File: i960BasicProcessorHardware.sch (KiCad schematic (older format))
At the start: 66 parts, among them J1 Conn_01x08, J10 Conn_01x03, J2 Conn_02x39_Odd_Even, J3 Conn_01x03, J4 Conn_02x05_Odd_Even, J5 Conn_02x05_Odd_Even, J6 Conn_02x05_Odd_Even, J7 Conn_01x06, J8 Conn_01x06, J9 Conn_01x12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

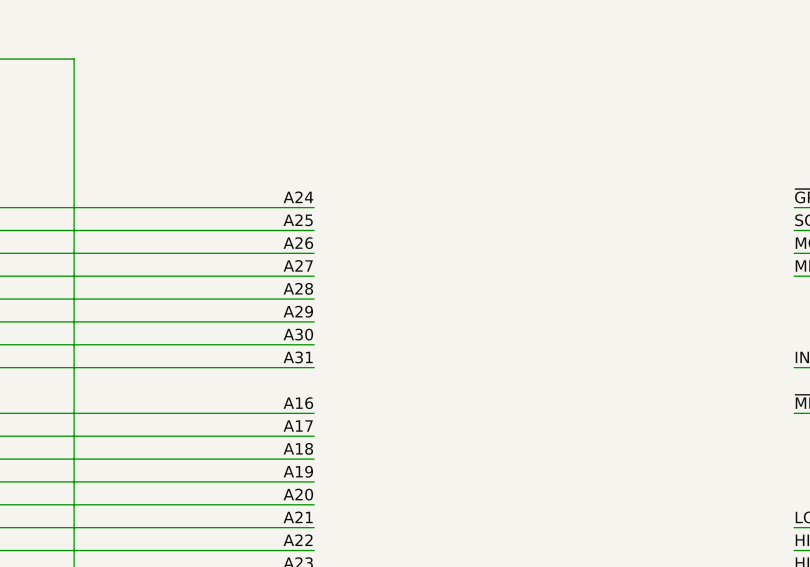
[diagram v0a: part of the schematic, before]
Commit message: Decided to break the highest 8 bits of the address out to a separate header.
I've done it before when I made the processor card interface. I can
position it fairly close without fear of signal degredation
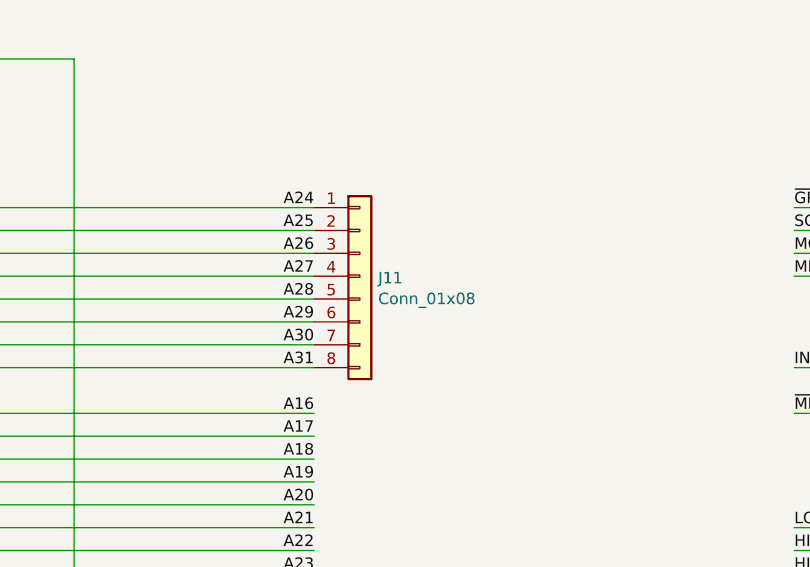
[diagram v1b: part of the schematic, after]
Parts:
- added J11: Conn_01x08, Connector_PinHeader_2.54mm:PinHeader_1x08_P2.54mm_Vertical, symbol Connector_Generic:Conn_01x08
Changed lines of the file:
@@
 NoConn ~ 14900 16000
 NoConn ~ 14900 16100
+$Comp
+L Connector_Generic:Conn_01x08 J11
+U 1 1 782AFBD5
+P 9000 16000
+F 0 "J11" H 9080 15992 50  0000 L CNN
+F 1 "Conn_01x08" H 9080 15901 50  0000 L CNN
+F 2 "Connector_PinHeader_2.54mm:PinHeader_1x08_P2.54mm_Vertical" H 9000 16000 50  0001 C CNN
+F 3 "~" H 9000 16000 50  0001 C CNN
+	1    9000 16000
+	1    0    0    -1
+$EndComp
 $EndSCHEMATC

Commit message: Rearrange some of the board and move the interrupt pull ups to individual resistors
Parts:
- added R3, R5: 10k, Resistor_SMD:R_0805_2012Metric_Pad1.20x1.40mm_HandSolder, symbol Device:R
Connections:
- wire segments 726 -> 730
- no-connect marks 89 -> 91
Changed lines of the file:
@@
 ALE
-Wire Wire Line
-	19200 17700 18200 17700
-Wire Wire Line
-	19200 17600 18200 17600
-Wire Wire Line
-	19200 17500 18200 17500
-Text Label 18200 17700 0    50   ~ 0
-BA1
-Text Label 18200 17600 0    50   ~ 0
-BA2
-Text Label 18200 17500 0    50   ~ 0
-BA3
 Wire Wire Line
 	13450 15800 14900 15800
@@
 Text Label 28000 21350 1    50   ~ 0
 ~RESET960
-Wire Wire Line
-	27600 20400 27600 21350
-Wire Wire Line
-	27500 20400 27500 21350
-Text Label 27500 21350 1    50   ~ 0
-~INT3
-Text Label 27600 21350 1    50   ~ 0
-~INT0
 Text Label 16050 15800 0    50   ~ 0
 GPA0
@@
 $EndComp
 Wire Wire Line
-	19200 17800 18200 17800
-Wire Wire Line
-	19200 17900 18200 17900
-Wire Wire Line
 	19200 17200 18200 17200
-Wire Wire Line
-	19200 18000 18200 18000
-Wire Wire Line
-	19200 18100 18200 18100
-Text Label 18200 17800 0    50   ~ 0
-HOLD_BREAKOUT
-Text Label 18200 17900 0    50   ~ 0
-HLDA
-Text Label 18200 18100 0    50   ~ 0
-~INT3
 NoConn ~ 14900 15800
 NoConn ~ 14900 15900
@@
 Text Label 15950 19000 0    50   ~ 0
 INT2_BREAKOUT
-Text Label 18200 18000 0    50   ~ 0
-INT2_BREAKOUT
 NoConn ~ 14900 16000
 NoConn ~ 14900 16100
@@
 	1    0    0    -1
 $EndComp
+Wire Wire Line
+	19200 17800 18200 17800
+Wire Wire Line
+	19200 17900 18200 17900
+Wire Wire Line
+	19200 18100 18200 18100
+Wire Wire Line
+	19200 18000 18200 18000
+Text Label 18200 17800 0    50   ~ 0
+HOLD_BREAKOUT
+Text Label 18200 17900 0    50   ~ 0
+HLDA
+Text Label 18200 18000 0    50   ~ 0
+~INT3
+Text Label 18200 18100 0    50   ~ 0
+INT2_BREAKOUT
+Text Label 18200 17500 0    50   ~ 0
+BA3
+Text Label 18200 17600 0    50   ~ 0
+BA2
+Text Label 18200 17700 0    50   ~ 0
+BA1
+Wire Wire Line
+	19200 17500 18200 17500
+Wire Wire Line
+	19200 17600 18200 17600
+Wire Wire Line
+	19200 17700 18200 17700
+$Comp
+L Device:R R?
+U 1 1 78683F66
+P 20800 12800
+AR Path="/629FB5E8/78683F66" Ref="R?"  Part="1"
+AR Path="/78683F66" Ref="R3"  Part="1"
+F 0 "R3" H 20870 12846 50  0000 L CNN
+F 1 "10k" H 20870 12755 50  0000 L CNN
+F 2 "Resistor_SMD:R_0805_2012Metric_Pad1.20x1.40mm_HandSolder" V 20730 12800 50  0001 C CNN
+F 3 "~" H 20800 12800 50  0001 C CNN
+	1    20800 12800
+	-1   0    0    1
+$EndComp
+Wire Wire Line
+	20800 12950 20800 13750
+$Comp
+L power:+5V #PWR?
+U 1 1 7873D22E
+P 20800 12450
+AR Path="/629FB5E8/7873D22E" Ref="#PWR?"  Part="1"
+AR Path="/7873D22E" Ref="#PWR052"  Part="1"
+F 0 "#PWR052" H 20800 12300 50  0001 C CNN
+F 1 "+5V" H 20815 12623 50  0000 C CNN
+F 2 "" H 20800 12450 50  0001 C CNN
+F 3 "" H 20800 12450 50  0001 C CNN
+	1    20800 12450
+	1    0    0    -1
+$EndComp
+Wire Wire Line
+	20800 12650 20800 12450
+Text Label 20800 13750 1    50   ~ 0
+~INT3
+Wire Wire Line
+	27500 20400 27500 21350
+Wire Wire Line
+	27600 20400 27600 21350
+NoConn ~ 27500 21350
+NoConn ~ 27600 21350
+$Comp
+L Device:R R?
+U 1 1 78AD08ED
+P 21150 12800
+AR Path="/629FB5E8/78AD08ED" Ref="R?"  Part="1"
+AR Path="/78AD08ED" Ref="R5"  Part="1"
+F 0 "R5" H 21220 12846 50  0000 L CNN
+F 1 "10k" H 21220 12755 50  0000 L CNN
+F 2 "Resistor_SMD:R_0805_2012Metric_Pad1.20x1.40mm_HandSolder" V 21080 12800 50  0001 C CNN
+F 3 "~" H 21150 12800 50  0001 C CNN
+	1    21150 12800
+	-1   0    0    1
+$EndComp
+Wire Wire Line
+	21150 12950 21150 13750
+$Comp
+L power:+5V #PWR?
+U 1 1 78AD08F4
+P 21150 12450
+AR Path="/629FB5E8/78AD08F4" Ref="#PWR?"  Part="1"
+AR Path="/78AD08F4" Ref="#PWR060"  Part="1"
+F 0 "#PWR060" H 21150 12300 50  0001 C CNN
+F 1 "+5V" H 21165 12623 50  0000 C CNN
+F 2 "" H 21150 12450 50  0001 C CNN
+F 3 "" H 21150 12450 50  0001 C CNN
+	1    21150 12450
+	1    0    0    -1
+$EndComp
+Wire Wire Line
+	21150 12650 21150 12450
+Text Label 21150 13750 1    50   ~ 0
+~INT0
 $EndSCHEMATC

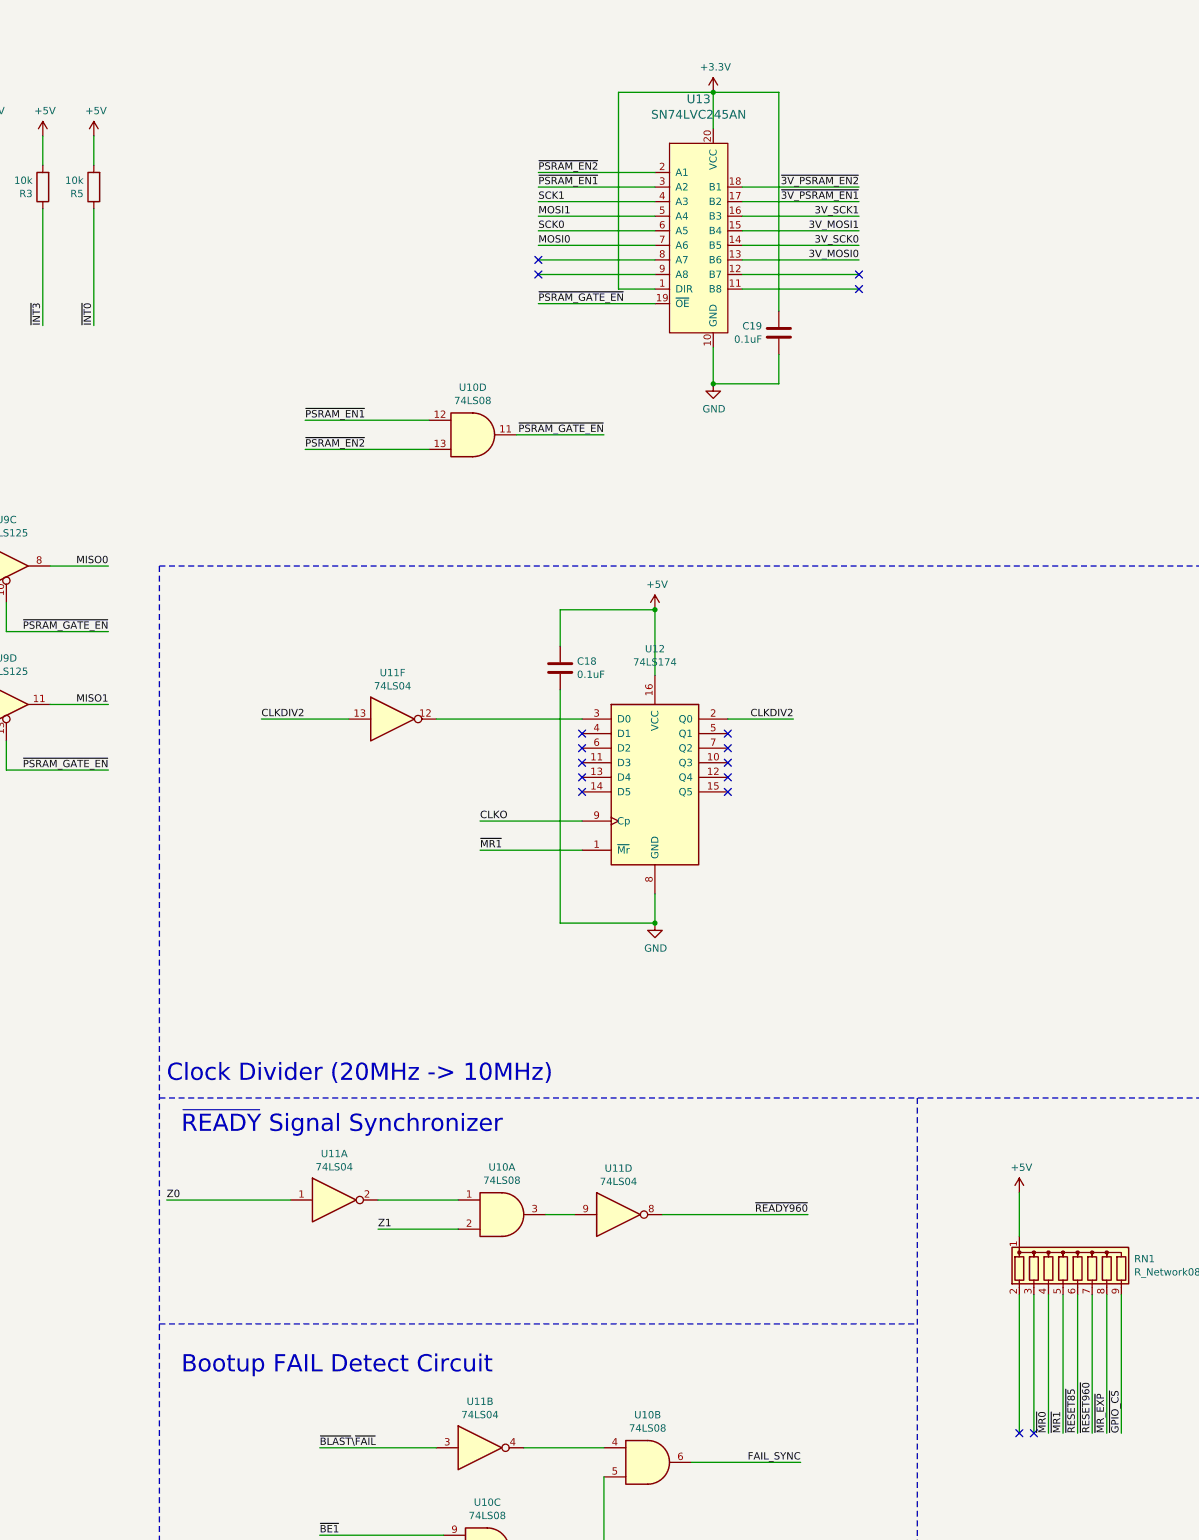
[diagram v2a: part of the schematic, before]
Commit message: Separate ~RESET960's pullup to a separate resistor
I have plenty of space underneath the plcc socket for resistors
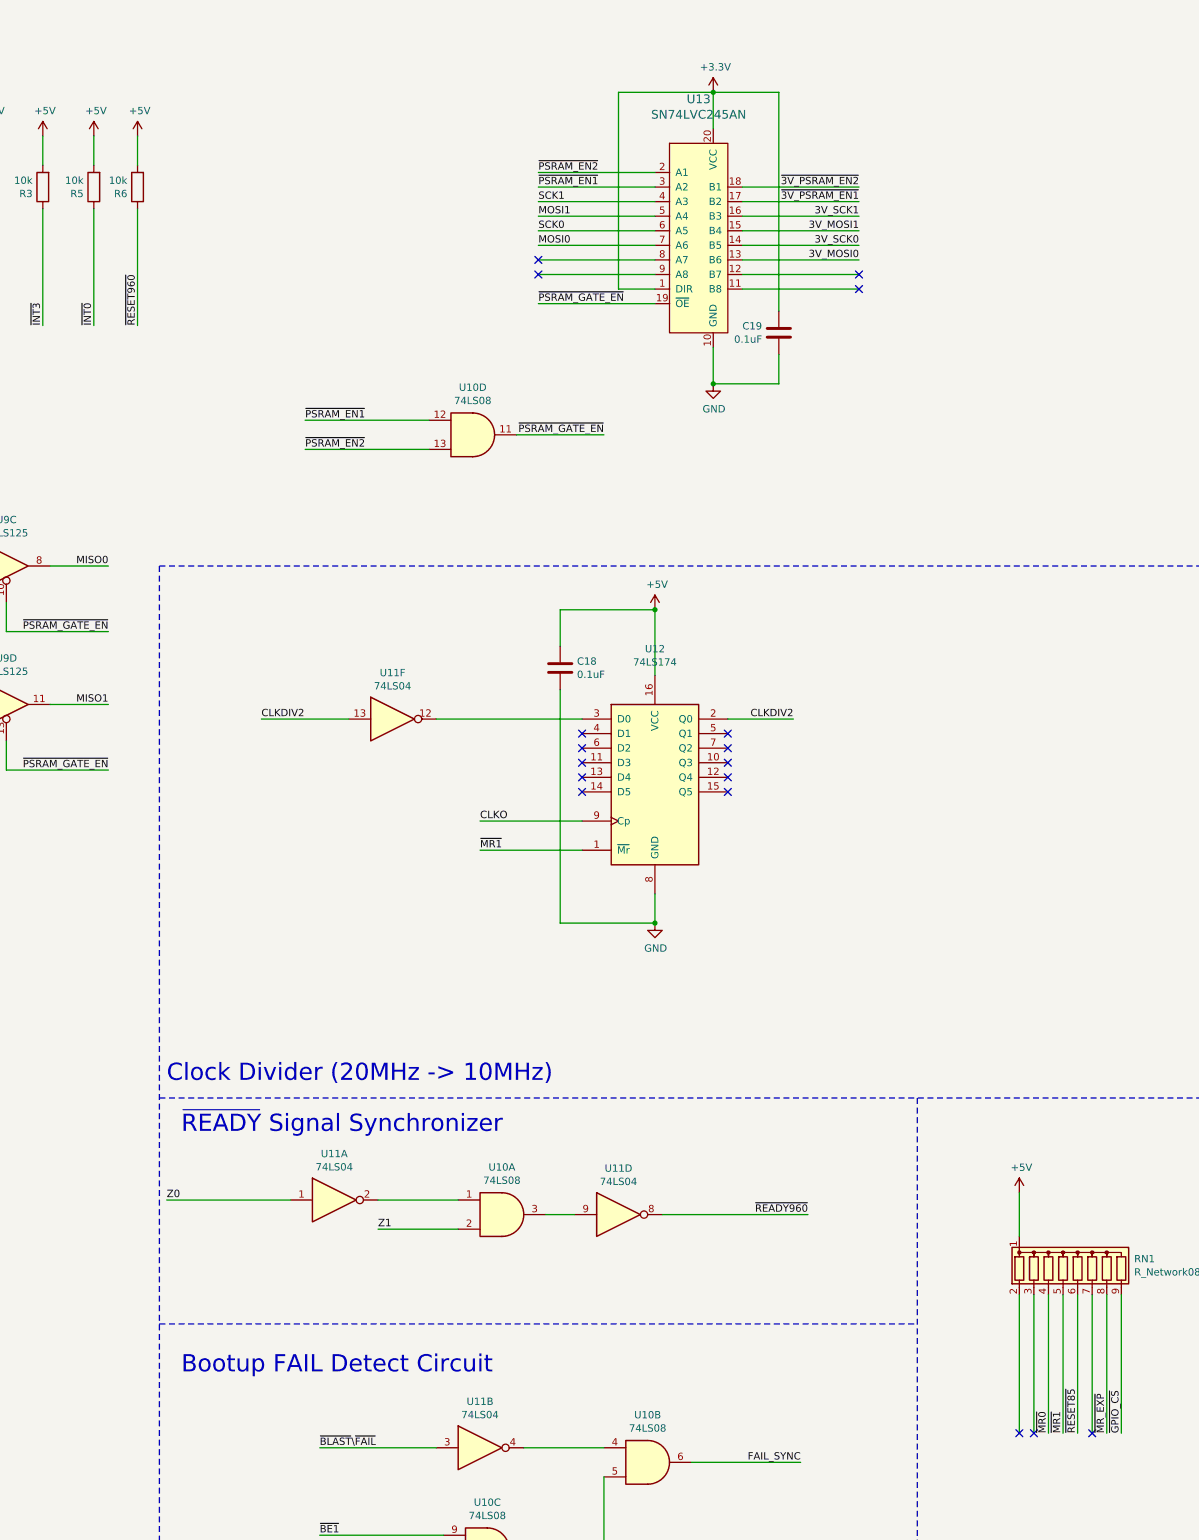
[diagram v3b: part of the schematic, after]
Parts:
- added R6: 10k, Resistor_SMD:R_0805_2012Metric_Pad1.20x1.40mm_HandSolder, symbol Device:R
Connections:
- wire segments 730 -> 732
- no-connect marks 91 -> 92
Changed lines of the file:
@@
 Text Label 28850 3450 0    50   ~ 0
 PA3
-Text Label 28000 21350 1    50   ~ 0
+Text Label 21450 13750 1    50   ~ 0
 ~RESET960
 Text Label 16050 15800 0    50   ~ 0
@@
 Text Label 21150 13750 1    50   ~ 0
 ~INT0
+$Comp
+L Device:R R?
+U 1 1 78BA1B0B
+P 21450 12800
+AR Path="/629FB5E8/78BA1B0B" Ref="R?"  Part="1"
+AR Path="/78BA1B0B" Ref="R6"  Part="1"
+F 0 "R6" H 21520 12846 50  0000 L CNN
+F 1 "10k" H 21520 12755 50  0000 L CNN
+F 2 "Resistor_SMD:R_0805_2012Metric_Pad1.20x1.40mm_HandSolder" V 21380 12800 50  0001 C CNN
+F 3 "~" H 21450 12800 50  0001 C CNN
+	1    21450 12800
+	-1   0    0    1
+$EndComp
+Wire Wire Line
+	21450 12950 21450 13750
+$Comp
+L power:+5V #PWR?
+U 1 1 78BA1B12
+P 21450 12450
+AR Path="/629FB5E8/78BA1B12" Ref="#PWR?"  Part="1"
+AR Path="/78BA1B12" Ref="#PWR061"  Part="1"
+F 0 "#PWR061" H 21450 12300 50  0001 C CNN
+F 1 "+5V" H 21465 12623 50  0000 C CNN
+F 2 "" H 21450 12450 50  0001 C CNN
+F 3 "" H 21450 12450 50  0001 C CNN
+	1    21450 12450
+	1    0    0    -1
+$EndComp
+Wire Wire Line
+	21450 12650 21450 12450
+NoConn ~ 28000 21350
 $EndSCHEMATC

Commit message: move ~RESET960 back to the primary chipset
also move ~INT3 to it as well. I want two different interrupt pins
accessible to the primary chipset. I have made the fourth ioexpander
completely exposed to the i960.
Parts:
- removed J1: Conn_01x08, Connector_PinHeader_2.54mm:PinHeader_1x08_P2.54mm_Vertical, symbol Connector_Generic:Conn_01x08
- removed J9: Conn_01x12, Connector_PinHeader_2.54mm:PinHeader_1x12_P2.54mm_Vertical, symbol Connector_Generic:Conn_01x12
- added J?: Conn_02x16_Odd_Even, symbol Connector_Generic:Conn_02x16_Odd_Even
- added J?: Conn_01x11, symbol Connector_Generic:Conn_01x11
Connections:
- net labels added: GPB0, GPB1, GPB2, GPB3, GPB4, GPB5, GPB6, GPB7
- net labels removed: PA2, PA3
- wire segments 732 -> 755
- no-connect marks 92 -> 85
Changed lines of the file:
@@
 Text Label 27150 7050 0    50   ~ 0
 SCK0
-Text Label 14900 15700 2    50   ~ 0
+Text Label 28850 3450 0    50   ~ 0
 ~RESET960
-$Comp
-L Connector_Generic:Conn_01x08 J1
-U 1 1 74CFC736
-P 17000 16100
-F 0 "J1" H 17080 16092 50  0000 L CNN
-F 1 "Conn_01x08" H 17080 16001 50  0000 L CNN
-F 2 "Connector_PinHeader_2.54mm:PinHeader_1x08_P2.54mm_Vertical" H 17000 16100 50  0001 C CNN
-F 3 "~" H 17000 16100 50  0001 C CNN
-	1    17000 16100
-	1    0    0    -1
-$EndComp
 Text Label 31450 3350 2    50   ~ 0
-PA2
-Text Label 31450 3450 2    50   ~ 0
-PA3
-Text Label 28850 3350 0    50   ~ 0
-PA2
-Text Label 28850 3450 0    50   ~ 0
-PA3
+~INT3
 Text Label 21450 13750 1    50   ~ 0
 ~RESET960
@@
 Text Label 15950 18000 0    50   ~ 0
 HOLD_BREAKOUT
-$Comp
-L Connector_Generic:Conn_01x12 J9
-U 1 1 76BFAED2
-P 19400 17500
-F 0 "J9" H 19480 17492 50  0000 L CNN
-F 1 "Conn_01x12" H 19480 17401 50  0000 L CNN
-F 2 "Connector_PinHeader_2.54mm:PinHeader_1x12_P2.54mm_Vertical" H 19400 17500 50  0001 C CNN
-F 3 "~" H 19400 17500 50  0001 C CNN
-	1    19400 17500
-	1    0    0    -1
-$EndComp
 Wire Wire Line
 	19200 17200 18200 17200
-NoConn ~ 14900 15800
-NoConn ~ 14900 15900
-NoConn ~ 14900 16200
-NoConn ~ 14900 16300
-NoConn ~ 14900 16400
 NoConn ~ 12050 16300
 $Comp
@@
 Text Label 15950 19000 0    50   ~ 0
 INT2_BREAKOUT
-NoConn ~ 14900 16000
-NoConn ~ 14900 16100
 $Comp
 L Connector_Generic:Conn_01x08 J11
@@
 	19200 17900 18200 17900
 Wire Wire Line
-	19200 18100 18200 18100
-Wire Wire Line
 	19200 18000 18200 18000
 Text Label 18200 17800 0    50   ~ 0
@@
 HLDA
 Text Label 18200 18000 0    50   ~ 0
-~INT3
-Text Label 18200 18100 0    50   ~ 0
 INT2_BREAKOUT
 Text Label 18200 17500 0    50   ~ 0
@@
 	21450 12650 21450 12450
 NoConn ~ 28000 21350
+Wire Wire Line
+	16800 16600 16050 16600
+Wire Wire Line
+	16800 16700 16050 16700
+Wire Wire Line
+	16800 16800 16050 16800
+Wire Wire Line
+	16800 16900 16050 16900
+Wire Wire Line
+	16800 17000 16050 17000
+Wire Wire Line
+	16800 17100 16050 17100
+Wire Wire Line
+	16800 17200 16050 17200
+Wire Wire Line
+	16800 17300 16050 17300
+Text Label 31450 3450 2    50   ~ 0
+~RESET960
+Text Label 28850 3350 0    50   ~ 0
+~INT3
+Text Label 14900 15700 2    50   ~ 0
+GPB0
+Text Label 14900 15800 2    50   ~ 0
+GPB1
+Text Label 14900 15900 2    50   ~ 0
+GPB2
+Text Label 14900 16000 2    50   ~ 0
+GPB3
+Text Label 14900 16100 2    50   ~ 0
+GPB4
+Text Label 14900 16200 2    50   ~ 0
+GPB5
+Text Label 14900 16300 2    50   ~ 0
+GPB6
+Text Label 14900 16400 2    50   ~ 0
+GPB7
+Text Label 16050 16600 0    50   ~ 0
+GPB0
+Text Label 16050 16700 0    50   ~ 0
+GPB1
+Text Label 16050 16800 0    50   ~ 0
+GPB2
+Text Label 16050 16900 0    50   ~ 0
+GPB3
+Text Label 16050 17000 0    50   ~ 0
+GPB4
+Text Label 16050 17100 0    50   ~ 0
+GPB5
+Text Label 16050 17200 0    50   ~ 0
+GPB6
+Text Label 16050 17300 0    50   ~ 0
+GPB7
+$Comp
+L Connector_Generic:Conn_02x16_Odd_Even J?
+U 1 1 79DF032E
+P 17000 16500
+F 0 "J?" H 17050 17417 50  0000 C CNN
+F 1 "Conn_02x16_Odd_Even" H 17050 17326 50  0000 C CNN
+F 2 "" H 17000 16500 50  0001 C CNN
+F 3 "~" H 17000 16500 50  0001 C CNN
+	1    17000 16500
+	1    0    0    -1
+$EndComp
+Wire Wire Line
+	17300 15800 18050 15800
+Wire Wire Line
+	17300 15900 18050 15900
+Wire Wire Line
+	17300 16000 18050 16000
+Wire Wire Line
+	17300 16100 18050 16100
+Wire Wire Line
+	17300 16200 18050 16200
+Wire Wire Line
+	17300 16300 18050 16300
+Wire Wire Line
+	17300 16400 18050 16400
+Wire Wire Line
+	17300 16500 18050 16500
+Text Label 18050 15800 2    50   ~ 0
+GPA0
+Text Label 18050 15900 2    50   ~ 0
+GPA1
+Text Label 18050 16000 2    50   ~ 0
+GPA2
+Text Label 18050 16100 2    50   ~ 0
+GPA3
+Text Label 18050 16200 2    50   ~ 0
+GPA4
+Text Label 18050 16300 2    50   ~ 0
+GPA5
+Text Label 18050 16400 2    50   ~ 0
+GPA6
+Text Label 18050 16500 2    50   ~ 0
+GPA7
+Wire Wire Line
+	17300 16600 18050 16600
+Wire Wire Line
+	17300 16700 18050 16700
+Wire Wire Line
+	17300 16800 18050 16800
+Wire Wire Line
+	17300 16900 18050 16900
+Wire Wire Line
+	17300 17000 18050 17000
+Wire Wire Line
+	17300 17100 18050 17100
+Wire Wire Line
+	17300 17200 18050 17200
+Wire Wire Line
+	17300 17300 18050 17300
+Text Label 18050 16600 2    50   ~ 0
+GPB0
+Text Label 18050 16700 2    50   ~ 0
+GPB1
+Text Label 18050 16800 2    50   ~ 0
+GPB2
+Text Label 18050 16900 2    50   ~ 0
+GPB3
+Text Label 18050 17000 2    50   ~ 0
+GPB4
+Text Label 18050 17100 2    50   ~ 0
+GPB5
+Text Label 18050 17200 2    50   ~ 0
+GPB6
+Text Label 18050 17300 2    50   ~ 0
+GPB7
+$Comp
+L Connector_Generic:Conn_01x11 J?
+U 1 1 79F7F59B
+P 19400 17500
+F 0 "J?" H 19480 17542 50  0000 L CNN
+F 1 "Conn_01x11" H 19480 17451 50  0000 L CNN
+F 2 "" H 19400 17500 50  0001 C CNN
+F 3 "~" H 19400 17500 50  0001 C CNN
+	1    19400 17500
+	1    0    0    -1
+$EndComp
 $EndSCHEMATC
